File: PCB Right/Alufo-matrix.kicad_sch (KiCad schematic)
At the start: 63 parts, among them K11 PG1350, K12 PG1350, K13 PG1350, K14 PG1350, K15 PG1350, K16 PG1350, K21 PG1350, K22 PG1350, K23 PG1350, K24 PG1350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

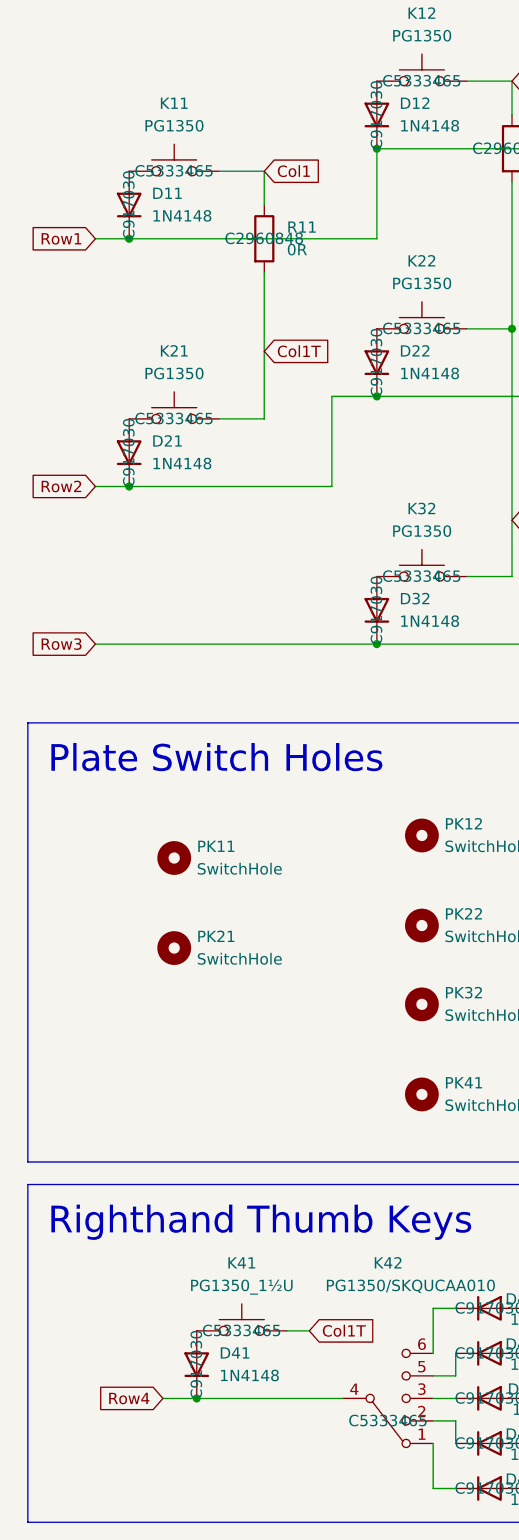
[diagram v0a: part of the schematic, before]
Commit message: Proof-of-concept: One USB C port on right side
The right hand PCB has been setup to have a single USB C port that can handle either bootloader duties or split connection via the side band channels.
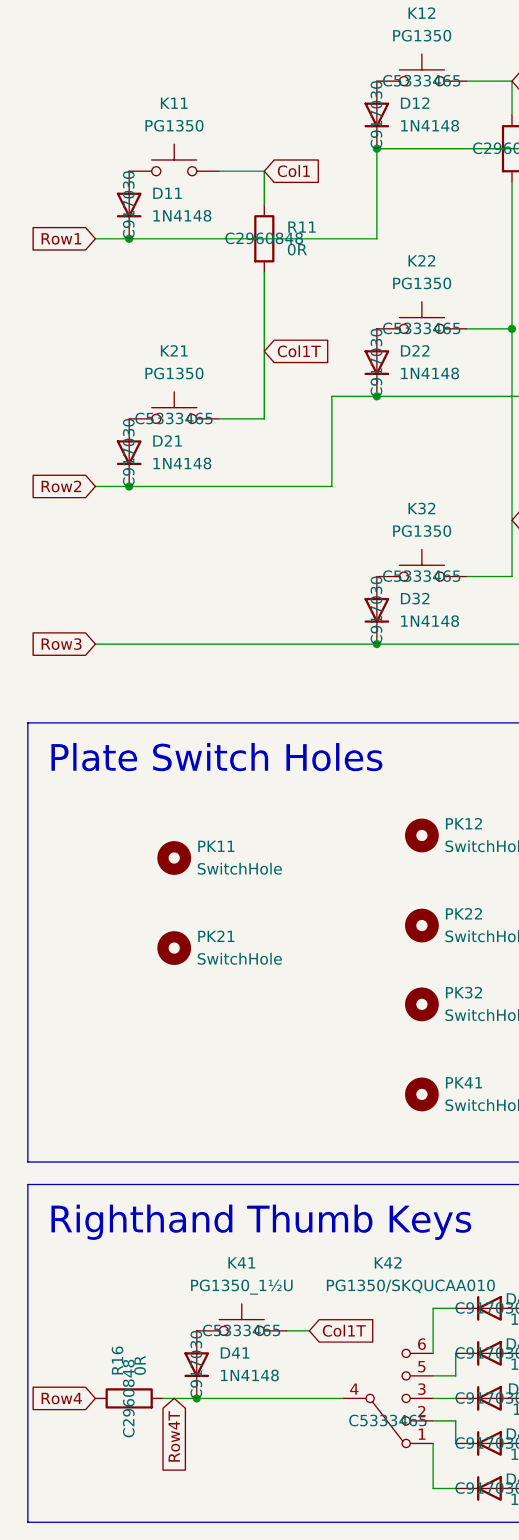
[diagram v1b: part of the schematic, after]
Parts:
- added R16: 0R, Resistor_SMD:R_2010_5025Metric, symbol Device:R
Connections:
- net Row4: now also R16.1; no longer D41.1 (K), K42.4 (Com)
- new net Row4T: D41.1 (K), K42.4 (Com), R16.2
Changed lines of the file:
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@@
 	(global_label "Row4"
 		(shape input)
-		(at 76.2 181.61 180)
+		(at 68.58 181.61 180)
 		(fields_autoplaced yes)
 		(effects
@@
 		)
 		(property "Intersheetrefs" "${INTERSHEET_REFS}"
-			(at 68.2558 181.61 0)
+			(at 60.6358 181.61 0)
 			(effects
 				(font
@@
 		)
 	)
+	(global_label "Row4T"
+		(shape input)
+		(at 77.47 181.61 270)
+		(fields_autoplaced yes)
+		(effects
+			(font
+				(size 1.27 1.27)
+			)
+			(justify right)
+		)
+		(property "Intersheetrefs" "${INTERSHEET_REFS}"
+			(at 77.47 189.5603 90)
+			(effects
+				(font
+					(size 1.27 1.27)
+				)
+				(justify right)
+				(hide yes)
+			)
+		)
+	)
 	(global_label "Col2"
 		(shape input)
@@
 					(size 1.27 1.27)
 				)
+				(hide yes)
 			)
 		)
@@
 					(unit 1)
 				)
+			)
+		)
+	)
+	(symbol
+		(lib_id "Device:R")
+		(at 72.39 181.61 90)
+		(unit 1)
+		(exclude_from_sim no)
+		(in_bom yes)
+		(on_board yes)
+		(dnp no)
+		(property "Reference" "R16"
+			(at 71.1199 179.07 0)
+			(effects
+				(font
+					(size 1.27 1.27)
+				)
+				(justify left)
+			)
+		)
+		(property "Value" "0R"
+			(at 73.6599 179.07 0)
+			(effects
+				(font
+					(size 1.27 1.27)
+				)
+				(justify left)
+			)
+		)
+		(property "Footprint" "Resistor_SMD:R_2010_5025Metric"
+			(at 72.39 183.388 90)
+			(effects
+				(font
+					(size 1.27 1.27)
+				)
+				(hide yes)
+			)
+		)
+		(property "Datasheet" "~"
+			(at 72.39 181.61 0)
+			(effects
+				(font
+					(size 1.27 1.27)
+				)
+				(hide yes)
+			)
+		)
+		(property "Description" "Resistor"
+			(at 72.39 181.61 0)
+			(effects
+				(font
+					(size 1.27 1.27)
+				)
+				(hide yes)
+			)
+		)
+		(property "LCSC" "C2960848"
+			(at 72.39 181.61 0)
+			(effects
+				(font
+					(size 1.27 1.27)
+				)
+			)
+		)
+		(pin "1"
+		)
+		(pin "2"
+		)
+		(instances
+			(project "Alufo"
+				(path "/52f043ac-ccff-4c85-bc10-2db9d3c9e3f3/ba0213d9-9934-4194-9bec-bf394cd27126"
+					(reference "R16")
+					(unit 1)
+				)
